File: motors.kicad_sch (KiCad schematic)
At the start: 0 parts

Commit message: Finish motor schematics.
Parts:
- added J14, J22: M1, Connector_JST:JST_XH_S8B-XH-A_1x08_P2.50mm_Horizontal, symbol Connector_Generic:Conn_01x08
- added J15: ENC1, Connector_Molex:Molex_PicoBlade_53261-0671_1x06-1MP_P1.25mm_Horizontal, symbol Connector_Generic_MountingPin:Conn_01x06_MountingPin
- added J16: M2, Connector_JST:JST_XH_S8B-XH-A_1x08_P2.50mm_Horizontal, symbol Connector_Generic:Conn_01x08
- added J17: ENC2, Connector_Molex:Molex_PicoBlade_53261-0671_1x06-1MP_P1.25mm_Horizontal, symbol Connector_Generic_MountingPin:Conn_01x06_MountingPin
- added J18: M3, Connector_JST:JST_XH_S8B-XH-A_1x08_P2.50mm_Horizontal, symbol Connector_Generic:Conn_01x08
- added J19: ENC3, Connector_Molex:Molex_PicoBlade_53261-0671_1x06-1MP_P1.25mm_Horizontal, symbol Connector_Generic_MountingPin:Conn_01x06_MountingPin
- added J2 (x5): SIGNAL, Connector_PinSocket_2.54mm:PinSocket_2x10_P2.54mm_Vertical, symbol Connector_Generic:Conn_02x10_Odd_Even
- added J20: M4, Connector_JST:JST_XH_S8B-XH-A_1x08_P2.50mm_Horizontal, symbol Connector_Generic:Conn_01x08
- added J21: ENC4, Connector_Molex:Molex_PicoBlade_53261-0671_1x06-1MP_P1.25mm_Horizontal, symbol Connector_Generic_MountingPin:Conn_01x06_MountingPin
- added J23: ENCD, Connector_Molex:Molex_PicoBlade_53261-0671_1x06-1MP_P1.25mm_Horizontal, symbol Connector_Generic_MountingPin:Conn_01x06_MountingPin
- added J3 (x5): PWR, Connector_PinSocket_2.54mm:PinSocket_1x10_P2.54mm_Vertical, symbol Connector_Generic:Conn_01x10
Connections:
- new net +24V: J3.1 (Pin_1), J3.1 (Pin_1), J3.1 (Pin_1), J3.1 (Pin_1), J3.1 (Pin_1), J3.2 (Pin_2), J3.2 (Pin_2), J3.2 (Pin_2), J3.2 (Pin_2), J3.2 (Pin_2)
- new net +3.3V: J2.3 (Pin_3), J2.3 (Pin_3), J2.3 (Pin_3), J2.3 (Pin_3), J2.3 (Pin_3)
- new net +5V: J14.5 (Pin_5), J15.6 (Pin_6), J16.5 (Pin_5), J17.6 (Pin_6), J18.5 (Pin_5), J19.6 (Pin_6), J2.1 (Pin_1), J2.1 (Pin_1), J2.1 (Pin_1), J2.1 (Pin_1), J2.1 (Pin_1), J20.5 (Pin_5), J21.6 (Pin_6), J22.5 (Pin_5), J23.6 (Pin_6)
- new net GND: J14.4 (Pin_4), J15.3 (Pin_3), J15.MP (MountPin), J16.4 (Pin_4), J17.3 (Pin_3), J17.MP (MountPin), J18.4 (Pin_4), J19.3 (Pin_3), J19.MP (MountPin), J2.16 (Pin_16), J2.16 (Pin_16), J2.16 (Pin_16), J2.16 (Pin_16), J2.16 (Pin_16), J2.18 (Pin_18), J2.18 (Pin_18), J2.18 (Pin_18), J2.18 (Pin_18), J2.18 (Pin_18), J2.20 (Pin_20), J2.20 (Pin_20), J2.20 (Pin_20), J2.20 (Pin_20), J2.20 (Pin_20), J20.4 (Pin_4), J21.3 (Pin_3), J21.MP (MountPin), J22.4 (Pin_4), J23.3 (Pin_3), J23.MP (MountPin), J3.3 (Pin_3), J3.3 (Pin_3), J3.3 (Pin_3), J3.3 (Pin_3), J3.3 (Pin_3), J3.4 (Pin_4), J3.4 (Pin_4), J3.4 (Pin_4), J3.4 (Pin_4), J3.4 (Pin_4)
- new net M1_CTRL_EN: J2.7 (Pin_7)
- new net M1_CTRL_STATUS: J2.5 (Pin_5)
- new net M1_DRV_FAULT: J2.19 (Pin_19)
- new net M1_ENC_A: J15.2 (Pin_2), J2.4 (Pin_4)
- new net M1_ENC_B: J15.5 (Pin_5), J2.6 (Pin_6)
- new net M1_ENC_C: J15.4 (Pin_4), J2.8 (Pin_8)
- new net M1_HALL_UX: J14.1 (Pin_1), J2.10 (Pin_10)
- new net M1_HALL_V: J14.2 (Pin_2), J2.12 (Pin_12)
- new net M1_HALL_WY: J14.3 (Pin_3), J2.14 (Pin_14)
- new net M1_U: J14.6 (Pin_6), J3.5 (Pin_5), J3.6 (Pin_6)
- new net M1_V: J14.7 (Pin_7), J3.7 (Pin_7), J3.8 (Pin_8)
- new net M1_W: J14.8 (Pin_8), J3.10 (Pin_10), J3.9 (Pin_9)
- new net M2_CTRL_EN: J2.7 (Pin_7)
- new net M2_CTRL_STATUS: J2.5 (Pin_5)
- new net M2_DRV_FAULT: J2.19 (Pin_19)
- new net M2_ENC_A: J17.2 (Pin_2), J2.4 (Pin_4)
- new net M2_ENC_B: J17.5 (Pin_5), J2.6 (Pin_6)
- new net M2_ENC_C: J17.4 (Pin_4), J2.8 (Pin_8)
- new net M2_HALL_UX: J16.1 (Pin_1), J2.10 (Pin_10)
- new net M2_HALL_V: J16.2 (Pin_2), J2.12 (Pin_12)
- new net M2_HALL_WY: J16.3 (Pin_3), J2.14 (Pin_14)
- new net M2_U: J16.6 (Pin_6), J3.5 (Pin_5), J3.6 (Pin_6)
- new net M2_V: J16.7 (Pin_7), J3.7 (Pin_7), J3.8 (Pin_8)
- new net M2_W: J16.8 (Pin_8), J3.10 (Pin_10), J3.9 (Pin_9)
- new net M3_CTRL_EN: J2.7 (Pin_7)
- new net M3_CTRL_STATUS: J2.5 (Pin_5)
- new net M3_DRV_FAULT: J2.19 (Pin_19)
- new net M3_ENC_A: J19.2 (Pin_2), J2.4 (Pin_4)
- new net M3_ENC_B: J19.5 (Pin_5), J2.6 (Pin_6)
- new net M3_ENC_C: J19.4 (Pin_4), J2.8 (Pin_8)
- new net M3_HALL_UX: J18.1 (Pin_1), J2.10 (Pin_10)
- new net M3_HALL_V: J18.2 (Pin_2), J2.12 (Pin_12)
- new net M3_HALL_WY: J18.3 (Pin_3), J2.14 (Pin_14)
- new net M3_U: J18.6 (Pin_6), J3.5 (Pin_5), J3.6 (Pin_6)
- new net M3_V: J18.7 (Pin_7), J3.7 (Pin_7), J3.8 (Pin_8)
- new net M3_W: J18.8 (Pin_8), J3.10 (Pin_10), J3.9 (Pin_9)
- new net M4_CTRL_EN: J2.7 (Pin_7)
- new net M4_CTRL_STATUS: J2.5 (Pin_5)
- new net M4_DRV_FAULT: J2.19 (Pin_19)
- new net M4_ENC_A: J2.4 (Pin_4), J21.2 (Pin_2)
- new net M4_ENC_B: J2.6 (Pin_6), J21.5 (Pin_5)
- new net M4_ENC_C: J2.8 (Pin_8), J21.4 (Pin_4)
- new net M4_HALL_UX: J2.10 (Pin_10), J20.1 (Pin_1)
- new net M4_HALL_V: J2.12 (Pin_12), J20.2 (Pin_2)
- new net M4_HALL_WY: J2.14 (Pin_14), J20.3 (Pin_3)
- new net M4_U: J20.6 (Pin_6), J3.5 (Pin_5), J3.6 (Pin_6)
- new net M4_V: J20.7 (Pin_7), J3.7 (Pin_7), J3.8 (Pin_8)
- new net M4_W: J20.8 (Pin_8), J3.10 (Pin_10), J3.9 (Pin_9)
- new net MD_CTRL_EN: J2.7 (Pin_7)
- new net MD_CTRL_STATUS: J2.5 (Pin_5)
- new net MD_DRV_FAULT: J2.19 (Pin_19)
- new net MD_ENC_A: J2.4 (Pin_4), J23.2 (Pin_2)
- new net MD_ENC_B: J2.6 (Pin_6), J23.5 (Pin_5)
- new net MD_ENC_C: J2.8 (Pin_8), J23.4 (Pin_4)
- new net MD_HALL_UX: J2.10 (Pin_10), J22.1 (Pin_1)
- new net MD_HALL_V: J2.12 (Pin_12), J22.2 (Pin_2)
- new net MD_HALL_WY: J2.14 (Pin_14), J22.3 (Pin_3)
- new net MD_U: J22.6 (Pin_6), J3.5 (Pin_5), J3.6 (Pin_6)
- new net MD_V: J22.7 (Pin_7), J3.7 (Pin_7), J3.8 (Pin_8)
- new net MD_W: J22.8 (Pin_8), J3.10 (Pin_10), J3.9 (Pin_9)
- new net M_SPI_MISO: J2.15 (Pin_15), J2.15 (Pin_15), J2.15 (Pin_15), J2.15 (Pin_15), J2.15 (Pin_15)
- new net M_SPI_MOSI: J2.13 (Pin_13), J2.13 (Pin_13), J2.13 (Pin_13), J2.13 (Pin_13), J2.13 (Pin_13)
- new net M_SPI_SCK: J2.11 (Pin_11), J2.11 (Pin_11), J2.11 (Pin_11), J2.11 (Pin_11), J2.11 (Pin_11)
- new net ~{M1_CS_CTRL}: J2.9 (Pin_9)
- new net ~{M1_CS_DRV}: J2.17 (Pin_17)
- new net ~{M2_CS_CTRL}: J2.9 (Pin_9)
- new net ~{M2_CS_DRV}: J2.17 (Pin_17)
- new net ~{M3_CS_CTRL}: J2.9 (Pin_9)
- new net ~{M3_CS_DRV}: J2.17 (Pin_17)
- new net ~{M4_CS_CTRL}: J2.9 (Pin_9)
- new net ~{M4_CS_DRV}: J2.17 (Pin_17)
- new net ~{MD_CS_CTRL}: J2.9 (Pin_9)
- new net ~{MD_CS_DRV}: J2.17 (Pin_17)
- no-connect marks 0 -> 10
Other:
- note added: "M1 Driver"
- note added: "M1 connectors"
- note added: "M2 Driver"
- note added: "M2 connectors"
- note added: "M3 Driver"
- note added: "M3 connectors"
- note added: "M4 Driver"
- note added: "M4 connectors"
- note added: "MD Driver"
- note added: "MD connectors"

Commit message: Import the previous main board to match the overall shape, and re-annotate the schematic.
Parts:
- renumbered J15 to J705, J17 to J706, J14 to J707, J16 to J708, J19 to J711, J21 to J712, J18 to J713, J20 to J714, J23 to J717, J22 to J718

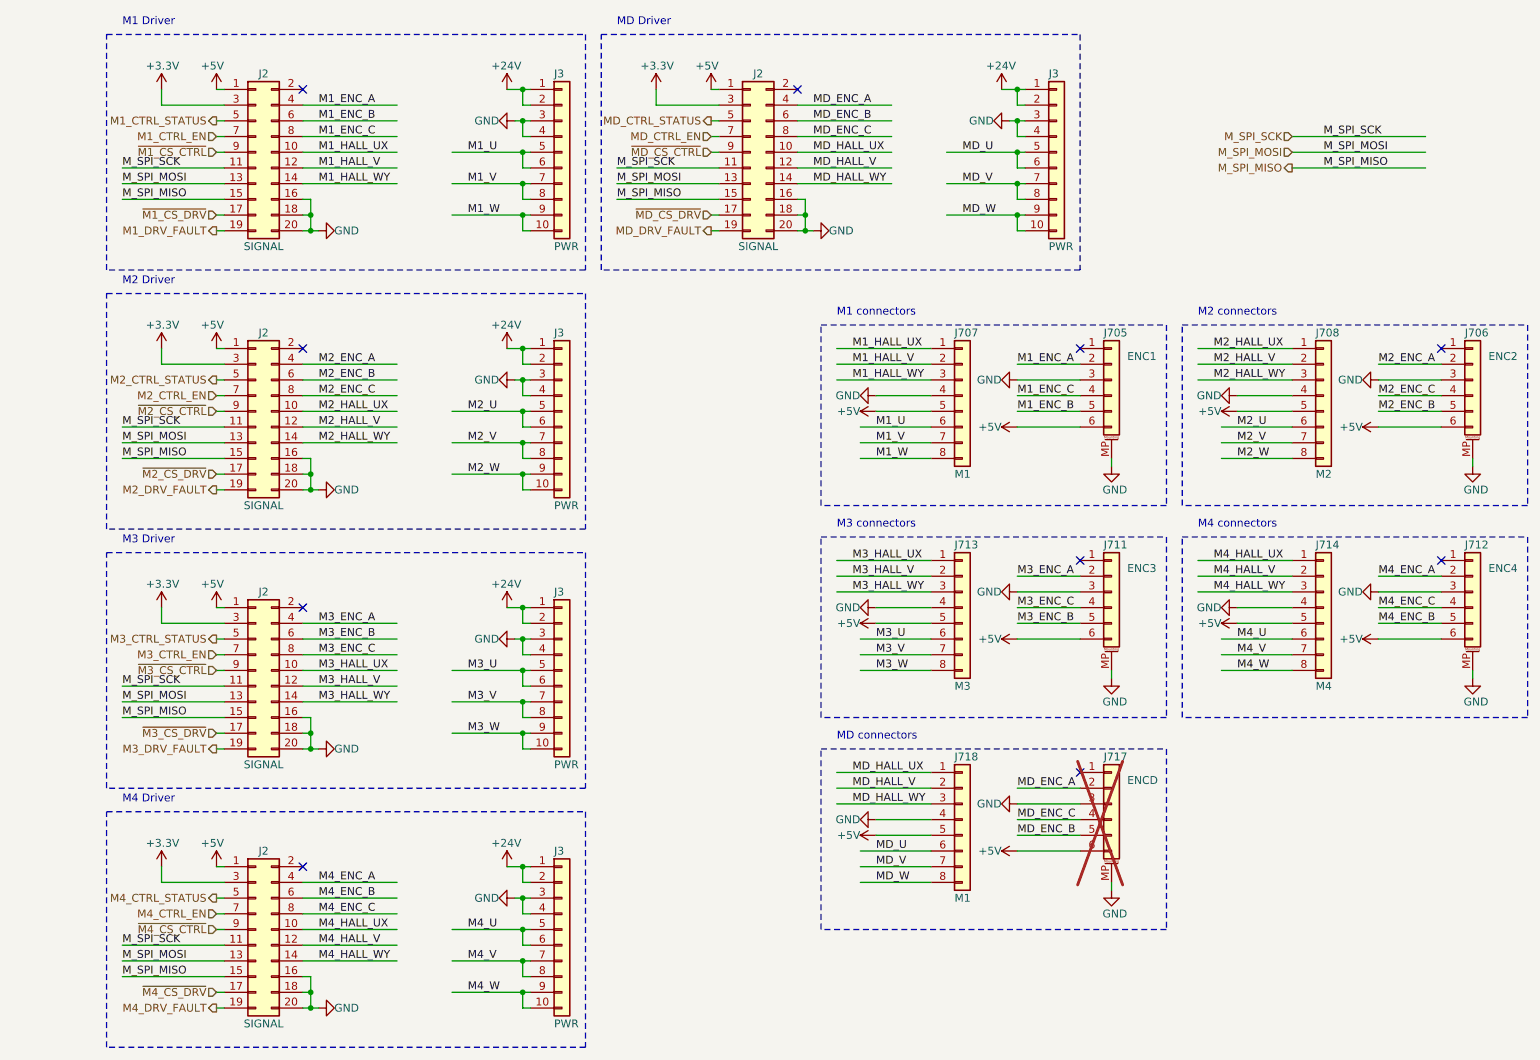
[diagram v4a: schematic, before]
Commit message: Start placing parts on pcb.
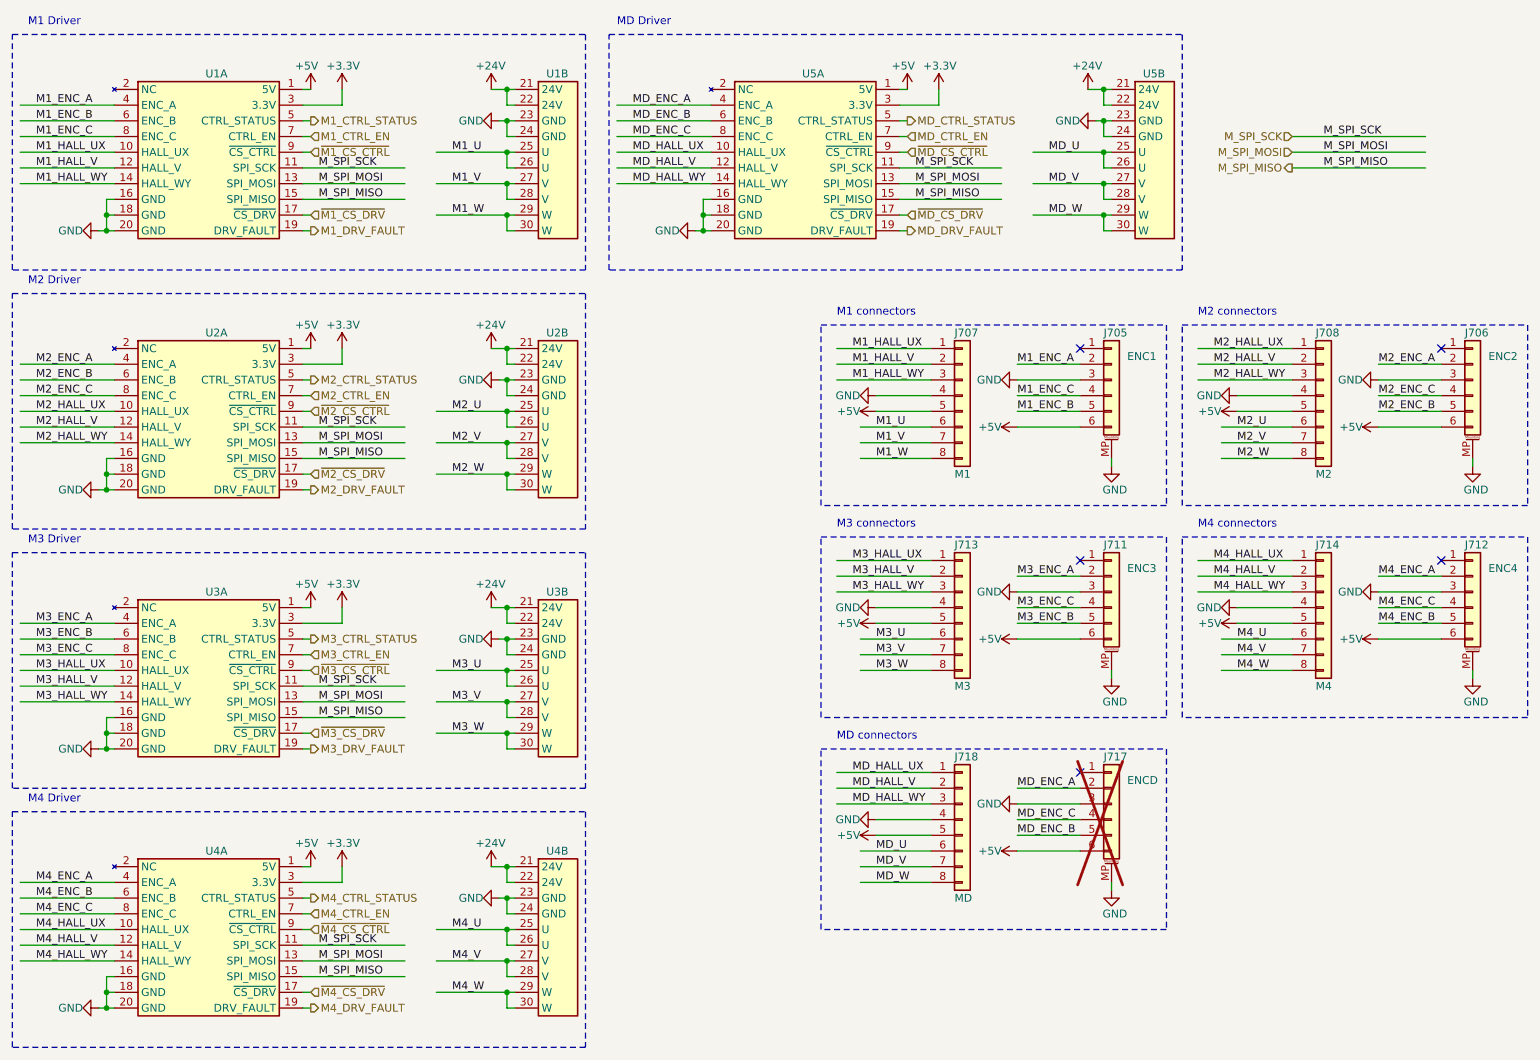
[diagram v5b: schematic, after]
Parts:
- removed J2 (x5): SIGNAL, Connector_PinSocket_2.54mm:PinSocket_2x10_P2.54mm_Vertical, symbol Connector_Generic:Conn_02x10_Odd_Even
- removed J3 (x5): PWR, Connector_PinSocket_2.54mm:PinSocket_1x10_P2.54mm_Vertical, symbol Connector_Generic:Conn_01x10
- added U1, U2, U3, U4, U5: ~, Immortals:motor-driver, symbol Immortals:MotorDriver
- J718: value M1 -> MD
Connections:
- net +24V: now also U1.21 (24V), U1.22 (24V), U2.21 (24V), U2.22 (24V), U3.21 (24V), U3.22 (24V), U4.21 (24V), U4.22 (24V), U5.21 (24V), U5.22 (24V)
- net +3.3V: now also U1.3 (3.3V), U2.3 (3.3V), U3.3 (3.3V), U4.3 (3.3V), U5.3 (3.3V)
- net +5V: now also U1.1 (5V), U2.1 (5V), U3.1 (5V), U4.1 (5V), U5.1 (5V)
- net GND: now also U1.16 (GND), U1.18 (GND), U1.20 (GND), U1.23 (GND), U1.24 (GND), U2.16 (GND), U2.18 (GND), U2.20 (GND), U2.23 (GND), U2.24 (GND), U3.16 (GND), U3.18 (GND), U3.20 (GND), U3.23 (GND), U3.24 (GND), U4.16 (GND), U4.18 (GND), U4.20 (GND), U4.23 (GND), U4.24 (GND), U5.16 (GND), U5.18 (GND), U5.20 (GND), U5.23 (GND), U5.24 (GND)
- net M1_CTRL_EN: now also U1.7 (CTRL_EN)
- net M1_CTRL_STATUS: now also U1.5 (CTRL_STATUS)
- net M1_DRV_FAULT: now also U1.19 (DRV_FAULT)
- net M1_ENC_A: now also U1.4 (ENC_A)
- net M1_ENC_B: now also U1.6 (ENC_B)
- net M1_ENC_C: now also U1.8 (ENC_C)
- net M1_HALL_UX: now also U1.10 (HALL_UX)
- net M1_HALL_V: now also U1.12 (HALL_V)
- net M1_HALL_WY: now also U1.14 (HALL_WY)
- net M1_U: now also U1.25 (U), U1.26 (U)
- net M1_V: now also U1.27 (V), U1.28 (V)
- net M1_W: now also U1.29 (W), U1.30 (W)
- net M2_CTRL_EN: now also U2.7 (CTRL_EN)
- net M2_CTRL_STATUS: now also U2.5 (CTRL_STATUS)
- net M2_DRV_FAULT: now also U2.19 (DRV_FAULT)
- net M2_ENC_A: now also U2.4 (ENC_A)
- net M2_ENC_B: now also U2.6 (ENC_B)
- net M2_ENC_C: now also U2.8 (ENC_C)
- net M2_HALL_UX: now also U2.10 (HALL_UX)
- net M2_HALL_V: now also U2.12 (HALL_V)
- net M2_HALL_WY: now also U2.14 (HALL_WY)
- net M2_U: now also U2.25 (U), U2.26 (U)
- net M2_V: now also U2.27 (V), U2.28 (V)
- net M2_W: now also U2.29 (W), U2.30 (W)
- net M3_CTRL_EN: now also U3.7 (CTRL_EN)
- net M3_CTRL_STATUS: now also U3.5 (CTRL_STATUS)
- net M3_DRV_FAULT: now also U3.19 (DRV_FAULT)
- net M3_ENC_A: now also U3.4 (ENC_A)
- net M3_ENC_B: now also U3.6 (ENC_B)
- net M3_ENC_C: now also U3.8 (ENC_C)
- net M3_HALL_UX: now also U3.10 (HALL_UX)
- net M3_HALL_V: now also U3.12 (HALL_V)
- net M3_HALL_WY: now also U3.14 (HALL_WY)
- net M3_U: now also U3.25 (U), U3.26 (U)
- net M3_V: now also U3.27 (V), U3.28 (V)
- net M3_W: now also U3.29 (W), U3.30 (W)
- net M4_CTRL_EN: now also U4.7 (CTRL_EN)
- net M4_CTRL_STATUS: now also U4.5 (CTRL_STATUS)
- net M4_DRV_FAULT: now also U4.19 (DRV_FAULT)
- net M4_ENC_A: now also U4.4 (ENC_A)
- net M4_ENC_B: now also U4.6 (ENC_B)
- net M4_ENC_C: now also U4.8 (ENC_C)
- net M4_HALL_UX: now also U4.10 (HALL_UX)
- net M4_HALL_V: now also U4.12 (HALL_V)
- net M4_HALL_WY: now also U4.14 (HALL_WY)
- net M4_U: now also U4.25 (U), U4.26 (U)
- net M4_V: now also U4.27 (V), U4.28 (V)
- net M4_W: now also U4.29 (W), U4.30 (W)
- net MD_CTRL_EN: now also U5.7 (CTRL_EN)
- net MD_CTRL_STATUS: now also U5.5 (CTRL_STATUS)
- net MD_DRV_FAULT: now also U5.19 (DRV_FAULT)
- net MD_ENC_A: now also U5.4 (ENC_A)
- net MD_ENC_B: now also U5.6 (ENC_B)
- net MD_ENC_C: now also U5.8 (ENC_C)
- net MD_HALL_UX: now also U5.10 (HALL_UX)
- net MD_HALL_V: now also U5.12 (HALL_V)
- net MD_HALL_WY: now also U5.14 (HALL_WY)
- net MD_U: now also U5.25 (U), U5.26 (U)
- net MD_V: now also U5.27 (V), U5.28 (V)
- net MD_W: now also U5.29 (W), U5.30 (W)
- net M_SPI_MISO: now also U1.15 (SPI_MISO), U2.15 (SPI_MISO), U3.15 (SPI_MISO), U4.15 (SPI_MISO), U5.15 (SPI_MISO)
- net M_SPI_MOSI: now also U1.13 (SPI_MOSI), U2.13 (SPI_MOSI), U3.13 (SPI_MOSI), U4.13 (SPI_MOSI), U5.13 (SPI_MOSI)
- net M_SPI_SCK: now also U1.11 (SPI_SCK), U2.11 (SPI_SCK), U3.11 (SPI_SCK), U4.11 (SPI_SCK), U5.11 (SPI_SCK)
- net ~{M1_CS_CTRL}: now also U1.9 (~{CS_CTRL})
- net ~{M1_CS_DRV}: now also U1.17 (~{CS_DRV})
- net ~{M2_CS_CTRL}: now also U2.9 (~{CS_CTRL})
- net ~{M2_CS_DRV}: now also U2.17 (~{CS_DRV})
- net ~{M3_CS_CTRL}: now also U3.9 (~{CS_CTRL})
- net ~{M3_CS_DRV}: now also U3.17 (~{CS_DRV})
- net ~{M4_CS_CTRL}: now also U4.9 (~{CS_CTRL})
- net ~{M4_CS_DRV}: now also U4.17 (~{CS_DRV})
- net ~{MD_CS_CTRL}: now also U5.9 (~{CS_CTRL})
- net ~{MD_CS_DRV}: now also U5.17 (~{CS_DRV})
- no-connect marks 10 -> 5

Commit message: Place all the components on the PCB.
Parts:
- U1, U2, U3, U4, U5: footprint Immortals:motor-driver -> Immortals:MotorDriver-SMT
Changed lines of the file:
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@@
       (effects (font (size 1.27 1.27)))
     )
-    (property "Footprint" "Immortals:motor-driver" (at 49.53 149.86 0)
+    (property "Footprint" "Immortals:MotorDriver-SMT" (at 49.53 149.86 0)
       (effects (font (size 1.27 1.27)) hide)
     )
@@
       (effects (font (size 1.27 1.27)))
     )
-    (property "Footprint" "Immortals:motor-driver" (at 146.05 24.13 0)
+    (property "Footprint" "Immortals:MotorDriver-SMT" (at 146.05 24.13 0)
       (effects (font (size 1.27 1.27)) hide)
     )
@@
       (effects (font (size 1.27 1.27)))
     )
-    (property "Footprint" "Immortals:motor-driver" (at 114.3 66.04 0)
+    (property "Footprint" "Immortals:MotorDriver-SMT" (at 114.3 66.04 0)
       (effects (font (size 1.27 1.27)) hide)
     )
@@
       (effects (font (size 1.27 1.27)))
     )
-    (property "Footprint" "Immortals:motor-driver" (at 49.53 107.95 0)
+    (property "Footprint" "Immortals:MotorDriver-SMT" (at 49.53 107.95 0)
       (effects (font (size 1.27 1.27)) hide)
     )
@@
       (effects (font (size 1.27 1.27)))
     )
-    (property "Footprint" "Immortals:motor-driver" (at 49.53 24.13 0)
+    (property "Footprint" "Immortals:MotorDriver-SMT" (at 49.53 24.13 0)
       (effects (font (size 1.27 1.27)) hide)
     )
@@
       (effects (font (size 1.27 1.27)))
     )
-    (property "Footprint" "Immortals:motor-driver" (at 114.3 24.13 0)
+    (property "Footprint" "Immortals:MotorDriver-SMT" (at 114.3 24.13 0)
       (effects (font (size 1.27 1.27)) hide)
     )
@@
       (effects (font (size 1.27 1.27)))
     )
-    (property "Footprint" "Immortals:motor-driver" (at 114.3 149.86 0)
+    (property "Footprint" "Immortals:MotorDriver-SMT" (at 114.3 149.86 0)
       (effects (font (size 1.27 1.27)) hide)
     )
@@
       (effects (font (size 1.27 1.27)))
     )
-    (property "Footprint" "Immortals:motor-driver" (at 114.3 107.95 0)
+    (property "Footprint" "Immortals:MotorDriver-SMT" (at 114.3 107.95 0)
       (effects (font (size 1.27 1.27)) hide)
     )
@@
       (effects (font (size 1.27 1.27)))
     )
-    (property "Footprint" "Immortals:motor-driver" (at 49.53 66.04 0)
+    (property "Footprint" "Immortals:MotorDriver-SMT" (at 49.53 66.04 0)
       (effects (font (size 1.27 1.27)) hide)
     )
@@
       (effects (font (size 1.27 1.27)))
     )
-    (property "Footprint" "Immortals:motor-driver" (at 210.82 24.13 0)
-      (effects (font (size 1.27 1.27)) hide)
-    )
+    (property "Footprint" "Immortals:MotorDriver-SMT" (at 210.82 24.13 0)
+      (effects (font (size 1.27 1.27)) hide)
+    )

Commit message: Fix motor winding order.
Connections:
- net M1_U: now also J707.8 (Pin_8); no longer J707.6 (Pin_6)
- net M1_W: now also J707.6 (Pin_6); no longer J707.8 (Pin_8)
- net M2_U: now also J708.8 (Pin_8); no longer J708.6 (Pin_6)
- net M2_W: now also J708.6 (Pin_6); no longer J708.8 (Pin_8)
- net M3_U: now also J713.8 (Pin_8); no longer J713.6 (Pin_6)
- net M3_W: now also J713.6 (Pin_6); no longer J713.8 (Pin_8)
- net M4_U: now also J714.8 (Pin_8); no longer J714.6 (Pin_6)
- net M4_W: now also J714.6 (Pin_6); no longer J714.8 (Pin_8)
- net MD_U: now also J718.8 (Pin_8); no longer J718.6 (Pin_6)
- net MD_W: now also J718.6 (Pin_6); no longer J718.8 (Pin_8)
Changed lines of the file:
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@@
     (effects (font (size 1.27 1.27)) (justify left bottom))
   )
-  (label "MD_U" (at 166.37 149.86 0) (fields_autoplaced)
+  (label "MD_U" (at 166.37 154.94 0) (fields_autoplaced)
     (effects (font (size 1.27 1.27)) (justify left bottom))
   )
@@
     (effects (font (size 1.27 1.27)) (justify left bottom))
   )
-  (label "M3_U" (at 166.37 115.57 0) (fields_autoplaced)
+  (label "M3_U" (at 166.37 120.65 0) (fields_autoplaced)
     (effects (font (size 1.27 1.27)) (justify left bottom))
   )
@@
     (effects (font (size 1.27 1.27)) (justify left bottom))
   )
-  (label "M4_W" (at 224.79 120.65 0) (fields_autoplaced)
+  (label "M4_W" (at 224.79 115.57 0) (fields_autoplaced)
     (effects (font (size 1.27 1.27)) (justify left bottom))
   )
@@
     (effects (font (size 1.27 1.27)) (justify left bottom))
   )
-  (label "M2_U" (at 224.79 81.28 0) (fields_autoplaced)
+  (label "M2_U" (at 224.79 86.36 0) (fields_autoplaced)
     (effects (font (size 1.27 1.27)) (justify left bottom))
   )
@@
     (effects (font (size 1.27 1.27)) (justify left bottom))
   )
-  (label "M2_W" (at 224.79 86.36 0) (fields_autoplaced)
+  (label "M2_W" (at 224.79 81.28 0) (fields_autoplaced)
     (effects (font (size 1.27 1.27)) (justify left bottom))
   )
@@
     (effects (font (size 1.27 1.27)) (justify left bottom))
   )
-  (label "M1_W" (at 166.37 86.36 0) (fields_autoplaced)
+  (label "M1_W" (at 166.37 81.28 0) (fields_autoplaced)
     (effects (font (size 1.27 1.27)) (justify left bottom))
   )
@@
     (effects (font (size 1.27 1.27)) (justify left bottom))
   )
-  (label "M1_U" (at 166.37 81.28 0) (fields_autoplaced)
+  (label "M1_U" (at 166.37 86.36 0) (fields_autoplaced)
     (effects (font (size 1.27 1.27)) (justify left bottom))
   )
@@
     (effects (font (size 1.27 1.27)) (justify left bottom))
   )
-  (label "MD_W" (at 166.37 154.94 0) (fields_autoplaced)
+  (label "MD_W" (at 166.37 149.86 0) (fields_autoplaced)
     (effects (font (size 1.27 1.27)) (justify left bottom))
   )
@@
     (effects (font (size 1.27 1.27)) (justify left bottom))
   )
-  (label "M3_W" (at 166.37 120.65 0) (fields_autoplaced)
+  (label "M3_W" (at 166.37 115.57 0) (fields_autoplaced)
     (effects (font (size 1.27 1.27)) (justify left bottom))
   )
@@
     (effects (font (size 1.27 1.27)) (justify left bottom))
   )
-  (label "M4_U" (at 224.79 115.57 0) (fields_autoplaced)
-    (effects (font (size 1.27 1.27)) (justify left bottom))
-  )
+  (label "M4_U" (at 224.79 120.65 0) (fields_autoplaced)
+    (effects (font (size 1.27 1.27)) (justify left bottom))
+  )
